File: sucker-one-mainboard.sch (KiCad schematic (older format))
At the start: 114 parts, among them J1 JST NC Valve, J10 JST Motor, J11 User Interface Module, J12 SWD, J2 JST NO Valve, J3 6P4C, J4 JST 3 Way Valve, J5 EXP Port, Q1 BSS138, Q2 BSS138, Q3 BSS138, Q4 DMN15H310SE-13, SW1 Power Switch, SW2 Reset, U1 LD1117S33TR, U2 TPS61087DRCR, U3 STM32F103RBTx, U4 2SMPP-03, U5 INA125UA, Y1 8MHz(16pf)

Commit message: Cleanup values
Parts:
- C12, C4, C8, C9: value 10uF 25V -> 10u 25V
- C15, C16: value 10uF 16v 1206 -> 10u 16v 1206
- C17: value 820pF -> 820p
- C18: value 1uF 16v 0603 -> 1u 16v 0603
- C19: value 100nF -> 100n
- C21: value 330uF 35v -> 330u 35v
- C22: value 0.1uF -> 0.1u
- C6, C7: value 20pF -> 20p
- R18: value R -> 100k
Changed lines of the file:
@@
 P 15450 9150
 F 0 "R18" H 15520 9196 50  0000 L CNN
-F 1 "R" H 15520 9105 50  0000 L CNN
+F 1 "100k" H 15520 9105 50  0000 L CNN
 F 2 "Resistor_SMD:R_0603_1608Metric_Pad0.98x0.95mm_HandSolder" V 15380 9150 50  0001 C CNN
 F 3 "~" H 15450 9150 50  0001 C CNN
@@
 P 4350 4900
 F 0 "C18" H 4235 4854 50  0000 R CNN
-F 1 "1uF 16v 0603" H 4235 4945 50  0000 R CNN
+F 1 "1u 16v 0603" H 4235 4945 50  0000 R CNN
 F 2 "Capacitor_SMD:C_0603_1608Metric_Pad1.08x0.95mm_HandSolder" H 4388 4750 50  0001 C CNN
 F 3 "~" H 4350 4900 50  0001 C CNN
@@
 P 4200 6550
 F 0 "C17" H 4085 6504 50  0000 R CNN
-F 1 "820pF" H 4085 6595 50  0000 R CNN
+F 1 "820p" H 4085 6595 50  0000 R CNN
 F 2 "Capacitor_SMD:C_0603_1608Metric_Pad1.08x0.95mm_HandSolder" H 4238 6400 50  0001 C CNN
 F 3 "~" H 4200 6550 50  0001 C CNN
@@
 P 3350 5350
 F 0 "C15" H 3550 5350 50  0000 R CNN
-F 1 "10uF 16v 1206" H 3950 5450 50  0000 R CNN
+F 1 "10u 16v 1206" H 3950 5450 50  0000 R CNN
 F 2 "Capacitor_SMD:C_1206_3216Metric_Pad1.33x1.80mm_HandSolder" H 3388 5200 50  0001 C CNN
 F 3 "~" H 3350 5350 50  0001 C CNN
@@
 P 3800 5350
 F 0 "C16" H 3700 5350 50  0000 R CNN
-F 1 "10uF 16v 1206" H 3750 5450 50  0000 R CNN
+F 1 "10u 16v 1206" H 3750 5450 50  0000 R CNN
 F 2 "Capacitor_SMD:C_1206_3216Metric_Pad1.33x1.80mm_HandSolder" H 3838 5200 50  0001 C CNN
 F 3 "~" H 3800 5350 50  0001 C CNN
@@
 P 1700 5500
 F 0 "C9" V 1650 5450 50  0000 R CNN
-F 1 "10uF 25V" V 1550 5600 50  0000 R CNN
+F 1 "10u 25V" V 1550 5600 50  0000 R CNN
 F 2 "Capacitor_SMD:C_0603_1608Metric_Pad1.08x0.95mm_HandSolder" H 1738 5350 50  0001 C CNN
 F 3 "~" H 1700 5500 50  0001 C CNN
@@
 P 1400 5500
 F 0 "C8" V 1350 5450 50  0000 R CNN
-F 1 "10uF 25V" V 1250 5600 50  0000 R CNN
+F 1 "10u 25V" V 1250 5600 50  0000 R CNN
 F 2 "Capacitor_SMD:C_0603_1608Metric_Pad1.08x0.95mm_HandSolder" H 1438 5350 50  0001 C CNN
 F 3 "~" H 1400 5500 50  0001 C CNN
@@
 P 1100 5500
 F 0 "C4" V 1050 5450 50  0000 R CNN
-F 1 "10uF 25V" V 950 5600 50  0000 R CNN
+F 1 "10u 25V" V 950 5600 50  0000 R CNN
 F 2 "Capacitor_SMD:C_0603_1608Metric_Pad1.08x0.95mm_HandSolder" H 1138 5350 50  0001 C CNN
 F 3 "~" H 1100 5500 50  0001 C CNN
@@
 P 2000 5500
 F 0 "C12" V 1950 5450 50  0000 R CNN
-F 1 "10uF 25V" V 1850 5600 50  0000 R CNN
+F 1 "10u 25V" V 1850 5600 50  0000 R CNN
 F 2 "Capacitor_SMD:C_0603_1608Metric_Pad1.08x0.95mm_HandSolder" H 2038 5350 50  0001 C CNN
 F 3 "~" H 2000 5500 50  0001 C CNN
@@
 P 1300 3700
 F 0 "C6" H 1415 3746 50  0000 L CNN
-F 1 "20pF" H 1415 3655 50  0000 L CNN
+F 1 "20p" H 1415 3655 50  0000 L CNN
 F 2 "Capacitor_SMD:C_0603_1608Metric_Pad1.08x0.95mm_HandSolder" H 1338 3550 50  0001 C CNN
 F 3 "~" H 1300 3700 50  0001 C CNN
@@
 P 1300 4250
 F 0 "C7" H 1415 4296 50  0000 L CNN
-F 1 "20pF" H 1415 4205 50  0000 L CNN
+F 1 "20p" H 1415 4205 50  0000 L CNN
 F 2 "Capacitor_SMD:C_0603_1608Metric_Pad1.08x0.95mm_HandSolder" H 1338 4100 50  0001 C CNN
 F 3 "~" H 1300 4250 50  0001 C CNN
@@
 P 5400 7250
 F 0 "C19" V 5285 7204 50  0000 R CNN
-F 1 "100nF" V 5200 7200 50  0000 R CNN
+F 1 "100n" V 5200 7200 50  0000 R CNN
 F 2 "Capacitor_SMD:C_0603_1608Metric_Pad1.08x0.95mm_HandSolder" H 5438 7100 50  0001 C CNN
 F 3 "~" H 5400 7250 50  0001 C CNN
@@
 P 9900 6350
 F 0 "C22" H 9785 6304 50  0000 R CNN
-F 1 "0.1uF" H 9785 6395 50  0000 R CNN
+F 1 "0.1u" H 9785 6395 50  0000 R CNN
 F 2 "Capacitor_SMD:C_0603_1608Metric_Pad1.08x0.95mm_HandSolder" H 9938 6200 50  0001 C CNN
 F 3 "~" H 9900 6350 50  0001 C CNN
@@
 P 10250 2050
 F 0 "C21" H 10368 2096 50  0000 L CNN
-F 1 "330uF 35v" H 10368 2005 50  0000 L CNN
+F 1 "330u 35v" H 10368 2005 50  0000 L CNN
 F 2 "Capacitor_SMD:CP_Elec_10x10" H 10288 1900 50  0001 C CNN
 F 3 "~" H 10250 2050 50  0001 C CNN

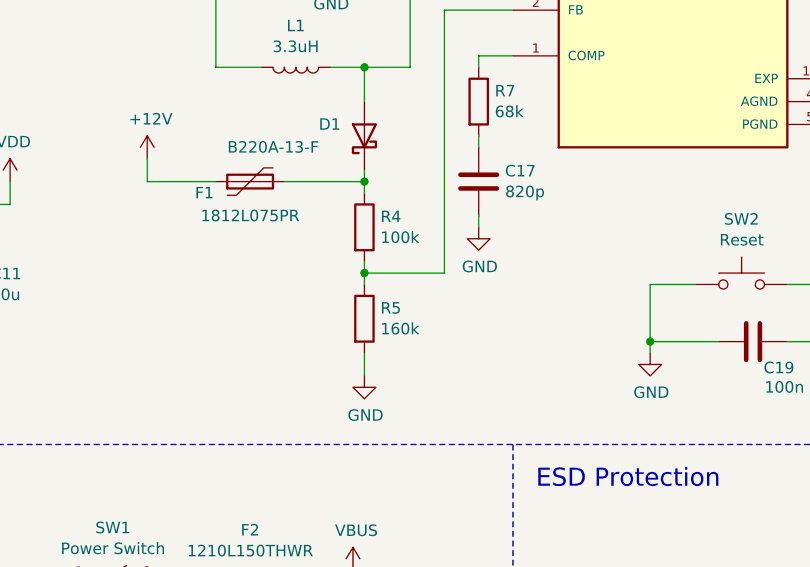
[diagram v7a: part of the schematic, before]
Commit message: Fix wrong boost feedback voltage divider resistors
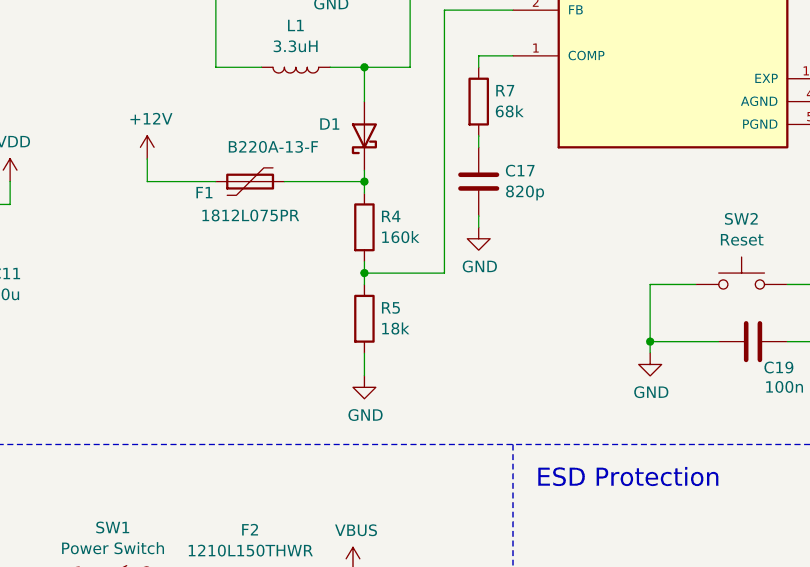
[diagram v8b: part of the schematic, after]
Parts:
- R4: value 100k -> 160k
- R5: value 160k -> 18k
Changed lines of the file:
@@
 P 3700 6750
 F 0 "R4" H 3770 6796 50  0000 L CNN
-F 1 "100k" H 3770 6705 50  0000 L CNN
+F 1 "160k" H 3770 6705 50  0000 L CNN
 F 2 "Resistor_SMD:R_0603_1608Metric_Pad0.98x0.95mm_HandSolder" V 3630 6750 50  0001 C CNN
 F 3 "~" H 3700 6750 50  0001 C CNN
@@
 P 3700 7150
 F 0 "R5" H 3770 7196 50  0000 L CNN
-F 1 "160k" H 3770 7105 50  0000 L CNN
+F 1 "18k" H 3770 7105 50  0000 L CNN
 F 2 "Resistor_SMD:R_0603_1608Metric_Pad0.98x0.95mm_HandSolder" V 3630 7150 50  0001 C CNN
 F 3 "~" H 3700 7150 50  0001 C CNN
